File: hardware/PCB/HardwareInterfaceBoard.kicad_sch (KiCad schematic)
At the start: 77 parts, among them J1 Relay Board Connector, J11 Feed Sensor R2, J14 Left LEDs, J15 Right LEDs, J16 Reset, J17 Shutdown, J2 Pi 5V, J20 EXT, J24 Raspberry Pi GPIO header, J25 RTC Header, J26 I2C0, J27 I2C1, J28 I2C2, J29 I2C3, J3 Display 5V, J30 I2C4, J31 I2C5, J32 I2C6, J33 I2C7, J4 DC 5V, J6 Feed Sensor L1, J7 Power bus, J8 Feed Sensor R1, J9 Feed Sensor L2, Q1 PN2222A, Q2 PN2222A, Q3 PN2222A, Q4 PN2222A, Q5 PN2222A, Q6 PN2222A, Q7 PN2222A, Q8 PN2222A, SW1 Pico Reset, U1 Raspberry Pico, U2 74HC595, U3 TCA9548A, U4 LM1117, U5 DS3231MZ, U6 74HC165, U7 74HC165

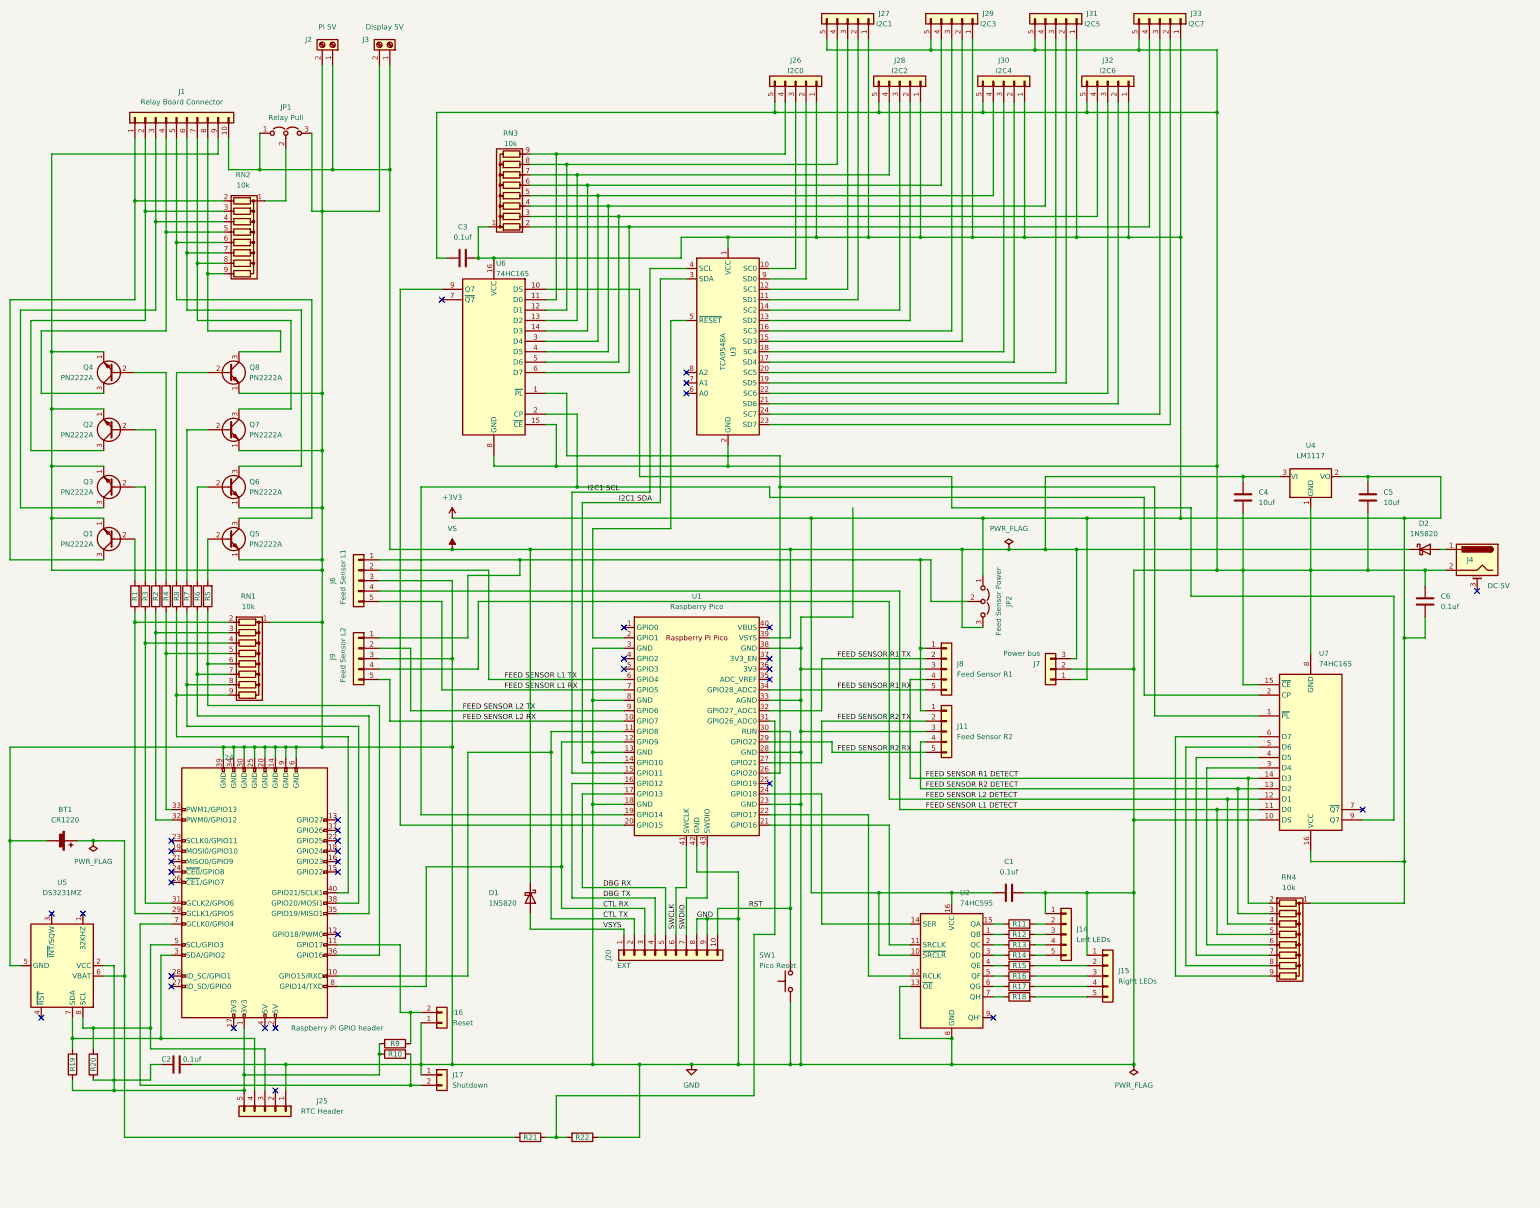
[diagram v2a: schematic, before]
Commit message: New board revision - main change is a better RTC battery sensing circuit. Also general board tidying/improvements, cleaned up the graphics folder, updated some graphics etc
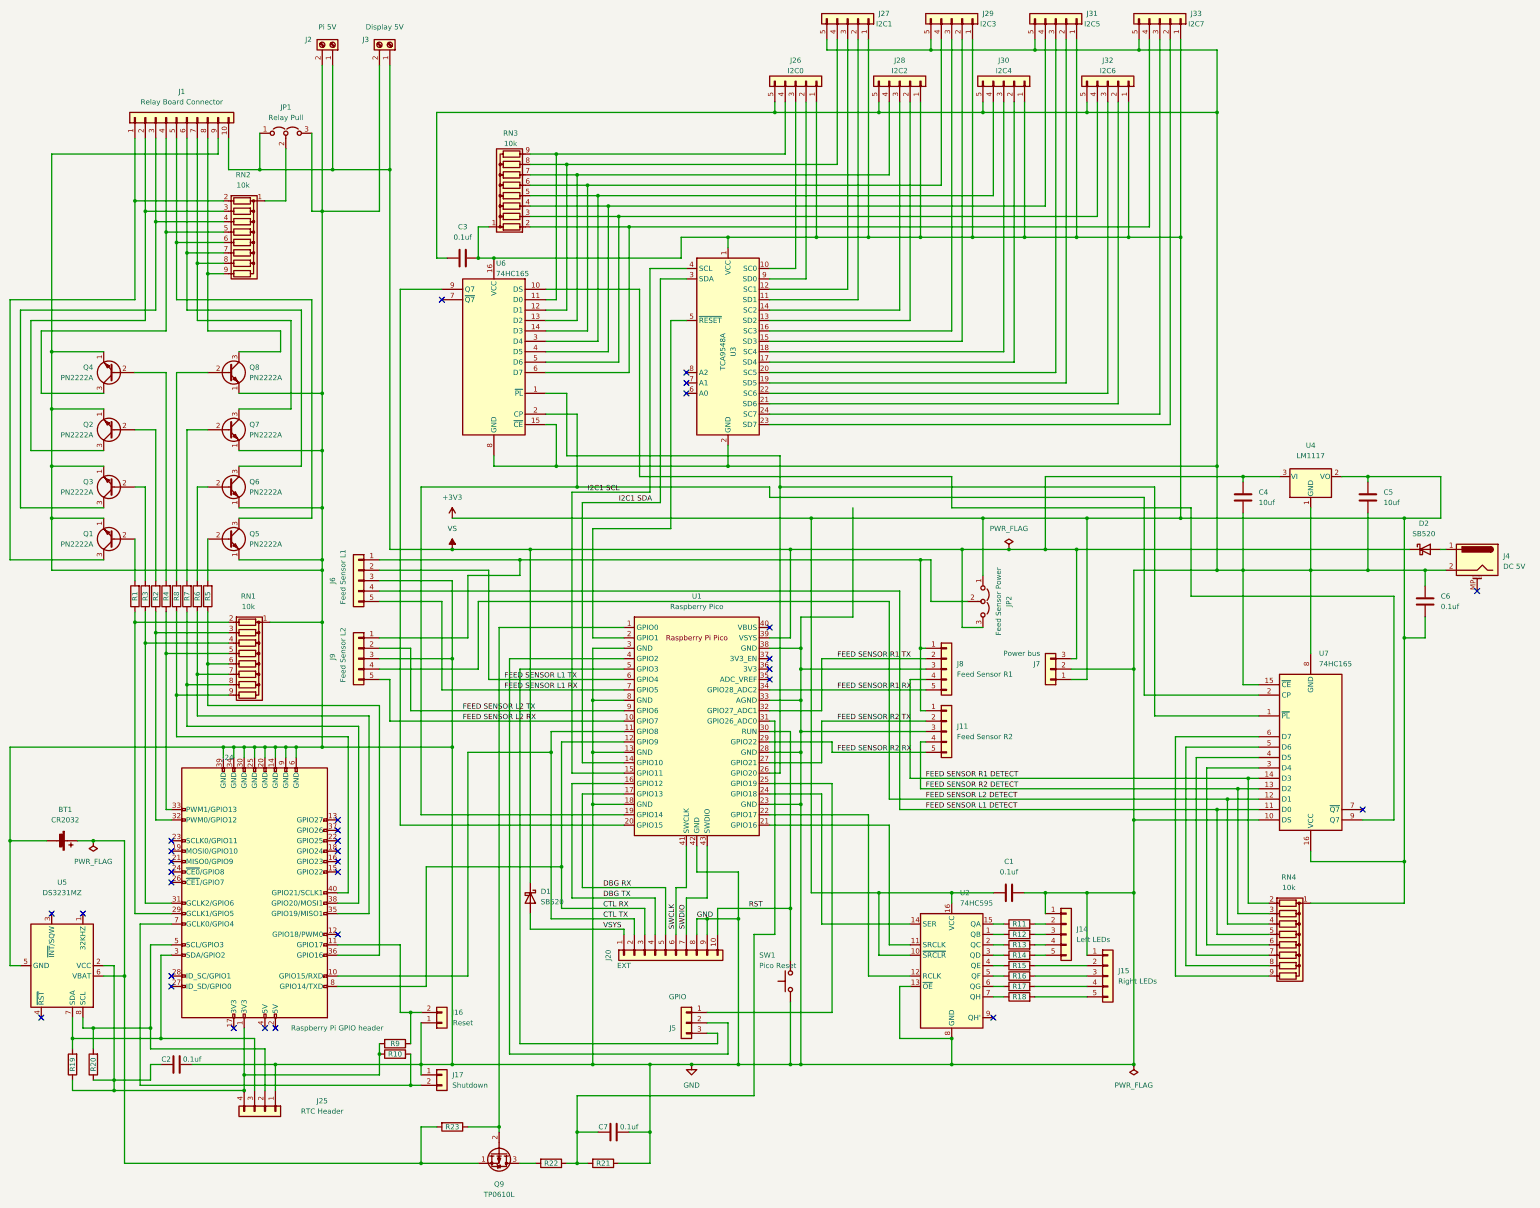
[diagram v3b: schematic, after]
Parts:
- removed D1, D2: 1N5820, Diode_THT:D_DO-201AD_P15.24mm_Horizontal, symbol Diode:1N5820
- added C7: 0.1uf, Capacitor_THT:C_Disc_D6.0mm_W2.5mm_P5.00mm, symbol Device:C
- added D1, D2: SB520, Diode_THT:D_DO-201AD_P15.24mm_Horizontal, symbol Diode:SB520
- added J5: GPIO, Connector_PinHeader_2.54mm:PinHeader_1x03_P2.54mm_Vertical, symbol Connector_Generic:Conn_01x03
- added Q9: TP0610L, Package_TO_SOT_THT:TO-92_Inline, symbol Transistor_FET:TP0610L
- added R23: 100k, Resistor_THT:R_Axial_DIN0207_L6.3mm_D2.5mm_P7.62mm_Horizontal, symbol Device:R
- BT1: value CR1220 -> CR2032; footprint Battery:BatteryHolder_Keystone_3000_1x12mm -> Battery:BatteryHolder_Keystone_1058_1x2032
- J25: footprint Connector_PinHeader_2.54mm:PinHeader_1x05_P2.54mm_Vertical -> Connector_PinHeader_2.54mm:PinHeader_1x04_P2.54mm_Vertical; symbol Connector_Generic:Conn_01x05 -> Connector_Generic:Conn_01x04
- J4: footprint Connector_BarrelJack:BarrelJack_Horizontal -> Connector_BarrelJack:BarrelJack_Horizontal_MP
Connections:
- net GND: now also R21.1, C7.2; no longer R22.1
- net VS: now also D1.1 (K), D2.1 (K)
- net VSYS: now also D1.2 (A)
- net at BT1.1 (+), U5.6 (VBAT): now also Q9.1 (S), R23.2; no longer R21.2
- net at C2.1, J24.1 (3V3), R10.1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: now also J25.4 (Pin_4); no longer J25.5 (Pin_5)
- net at J24.5 (SCL/GPIO3), R20.2, U5.8 (SCL): now also J25.2 (Pin_2); no longer J25.3 (Pin_3)
- net at J24.3 (SDA/GPIO2), R19.2, U5.7 (SDA): now also J25.3 (Pin_3); no longer J25.4 (Pin_4)
- net at J4.1: now also D2.2 (A)
- net at U1.1 (GPIO0): now also Q9.2 (G), R23.1
- net at U1.25 (GPIO19): now also J5.1 (Pin_1)
- net at U1.4 (GPIO2): now also J5.2 (Pin_2)
- net at U1.5 (GPIO3): now also J5.3 (Pin_3)
- new net: Q9.3 (D), R22.2
- new net: C7.1, R21.2, R22.1, U1.31 (GPIO26_ADC0)
- no-connect marks 36 -> 31
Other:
- moved on the sheet: R21, R22
